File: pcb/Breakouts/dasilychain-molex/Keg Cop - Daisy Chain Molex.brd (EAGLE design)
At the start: 33.2 x 43.2 mm, 4 parts

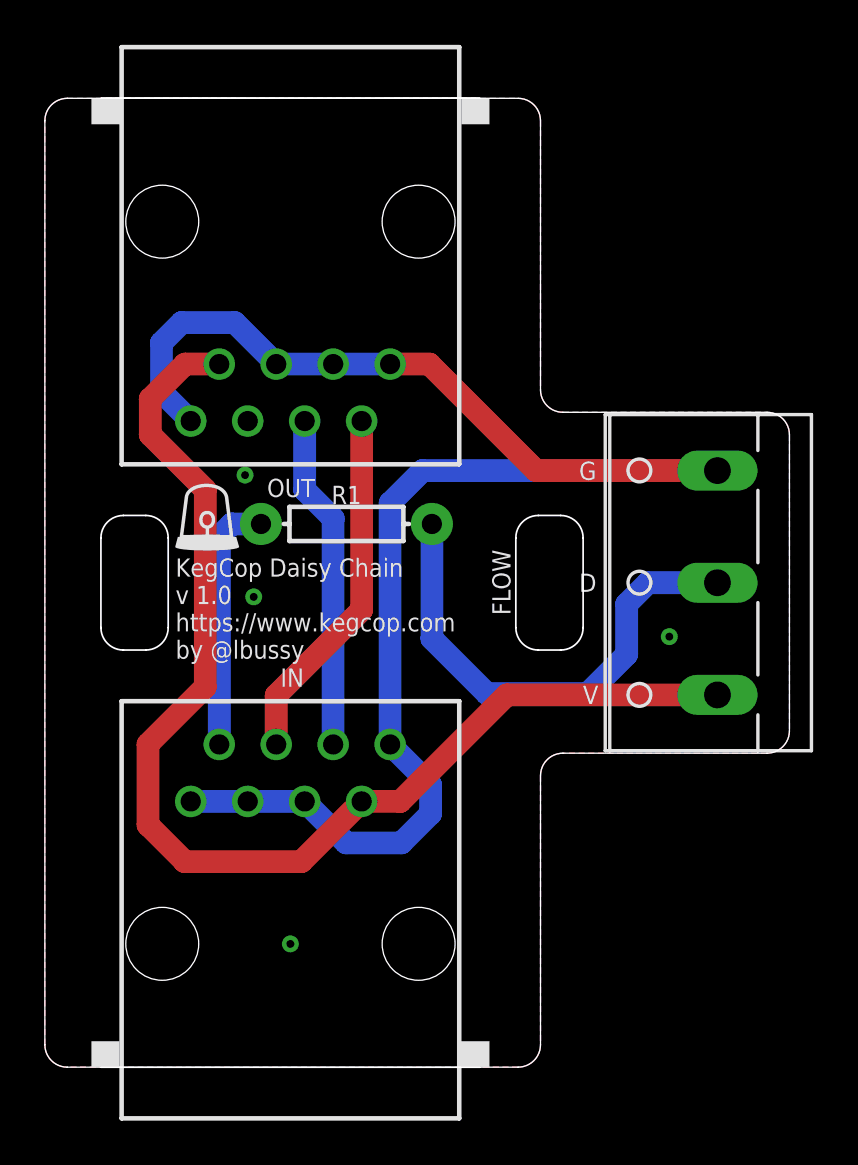
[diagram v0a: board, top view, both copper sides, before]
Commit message: Reorganize daisy chain boards
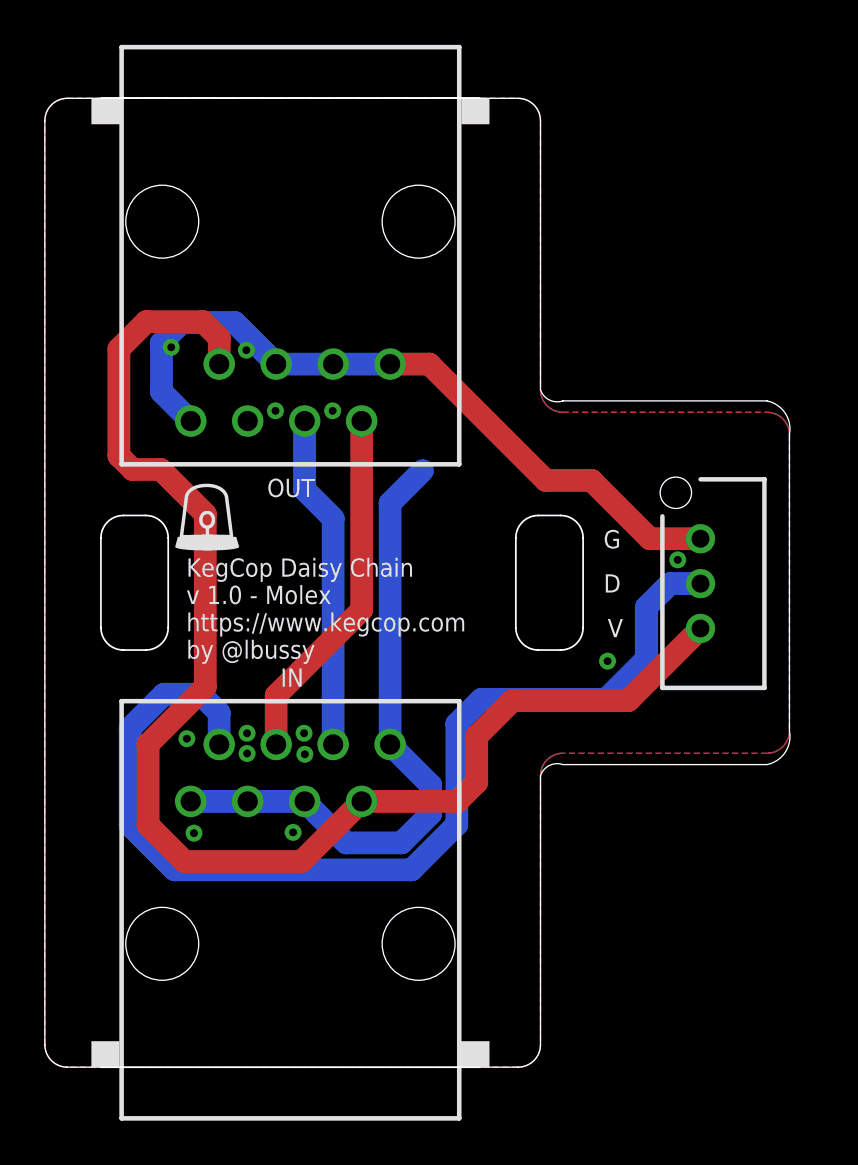
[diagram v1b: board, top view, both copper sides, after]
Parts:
- removed FLOW: (no value), con-wago-500:W237-103
- removed R1: 1k, SparkFun-Resistors:AXIAL-0.3
- added J1: 0533240360, SamacSys_Parts:0533240360
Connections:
- removed net N$1: FLOW.2, R1.P$2
- net 5VD: now also J1.3; no longer FLOW.1
- net DATA0: now also J1.2; no longer R1.P$1
- net GND: now also J1.1; no longer FLOW.3
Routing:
- net DATA0: track 11.4 -> 46.2 mm
- net N$1: track 22.2 -> 0.00 mm
- net GND: track 73.7 -> 61.1 mm, vias 4 -> 13
- net 5VD: track 53.9 -> 61.9 mm
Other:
- outline, holes or cut-outs redrawn
- board text added: "KegCop Daisy Chain v 1.0 - Molex https://www.kegcop.com by @lbussy"
- board text removed: "KegCop Daisy Chain v 1.0 https://www.kegcop.com by @lbussy"
